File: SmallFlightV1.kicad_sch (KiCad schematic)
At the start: 0 parts

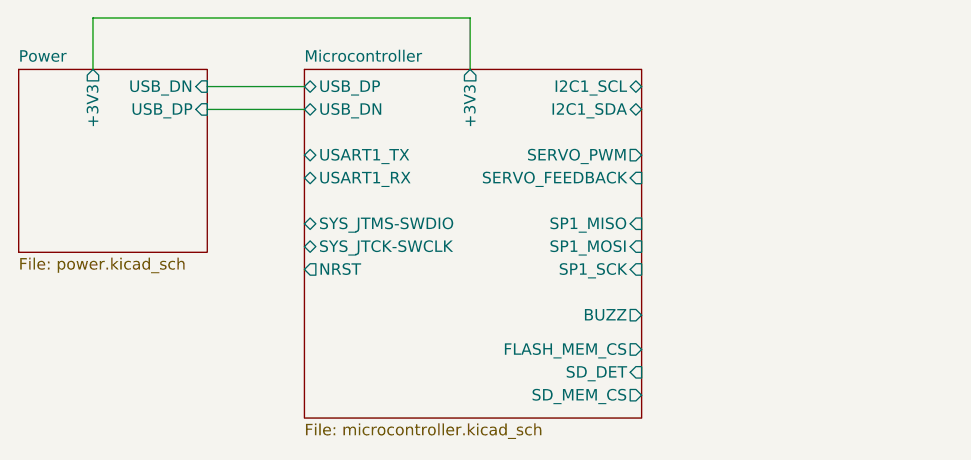
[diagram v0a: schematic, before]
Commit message: Update MCU schematic with VCAP capacitor. Draw boxes around communication busses and programming bus
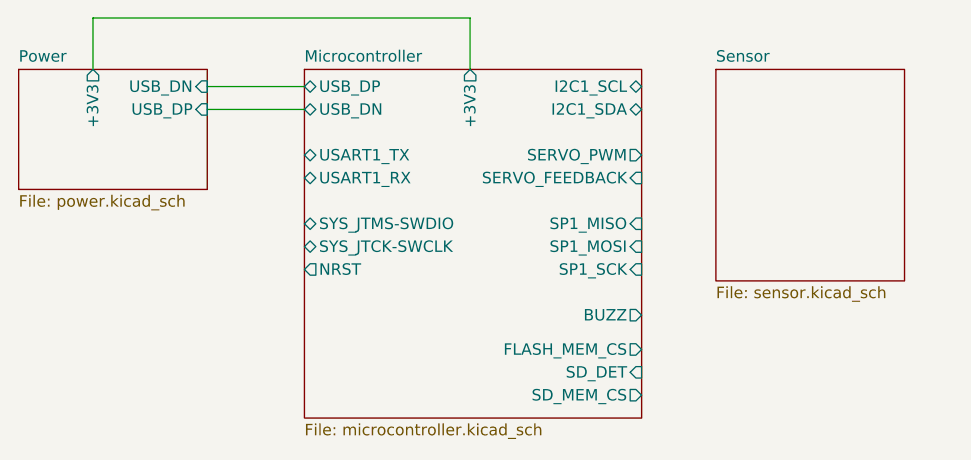
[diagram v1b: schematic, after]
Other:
- added sheet Sensor (sensor.kicad_sch)
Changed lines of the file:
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@@
 (kicad_sch
-	(version 20250114)
+	(version 20260306)
 	(generator "eeschema")
-	(generator_version "9.0")
+	(generator_version "10.0")
 	(paper "A4")
 	(wire
@@
 			(width 0)
 			(type default)
+		)
+	)
+	(sheet
+		(at 170.815 31.115)
+		(size 20.955 23.495)
+		(exclude_from_sim no)
+		(in_bom yes)
+		(on_board yes)
+		(dnp no)
+		(fields_autoplaced yes)
+		(stroke
+			(width 0.1524)
+			(type solid)
+		)
+		(fill
+			(color 0 0 0 0)
+		)
+		(property "Sheetname" "Sensor"
+			(at 170.815 30.4034 0)
+			(show_name no)
+			(do_not_autoplace no)
+			(effects
+				(font
+					(size 1.27 1.27)
+				)
+				(justify left bottom)
+			)
+		)
+		(property "Sheetfile" "sensor.kicad_sch"
+			(at 170.815 55.1946 0)
+			(show_name no)
+			(do_not_autoplace no)
+			(effects
+				(font
+					(size 1.27 1.27)
+				)
+				(justify left top)
+			)
+		)
+		(instances
+			(project "SmallFlightV1"
+				(path "/5a8b04a1-a6d6-48bd-ac5f-d4986cb92d03"
+					(page "4")
+				)
+			)
 		)
 	)
@@
 		)
 		(fill
-			(color 0 0 0 0.0000)
+			(color 0 0 0 0)
 		)
 		(property "Sheetname" "Microcontroller"
 			(at 125.095 30.4034 0)
+			(show_name no)
+			(do_not_autoplace no)
 			(effects
 				(font
@@
 		(property "Sheetfile" "microcontroller.kicad_sch"
 			(at 125.095 70.4346 0)
+			(show_name no)
+			(do_not_autoplace no)
 			(effects
 				(font
@@
 	(sheet
 		(at 93.345 31.115)
-		(size 20.955 20.32)
+		(size 20.955 13.335)
 		(exclude_from_sim no)
 		(in_bom yes)
@@
 		)
 		(fill
-			(color 0 0 0 0.0000)
+			(color 0 0 0 0)
 		)
 		(property "Sheetname" "Power"
 			(at 93.345 30.4034 0)
+			(show_name no)
+			(do_not_autoplace no)
 			(effects
 				(font
@@
 		)
 		(property "Sheetfile" "power.kicad_sch"
-			(at 93.345 52.0196 0)
-			(effects
-				(font
+			(at 93.345 45.0346 0)
+			(show_name no)
+			(do_not_autoplace no)
+			(effects
+				(font

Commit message: remove redundant stm32f44 document folder. remove USB pinouts and references
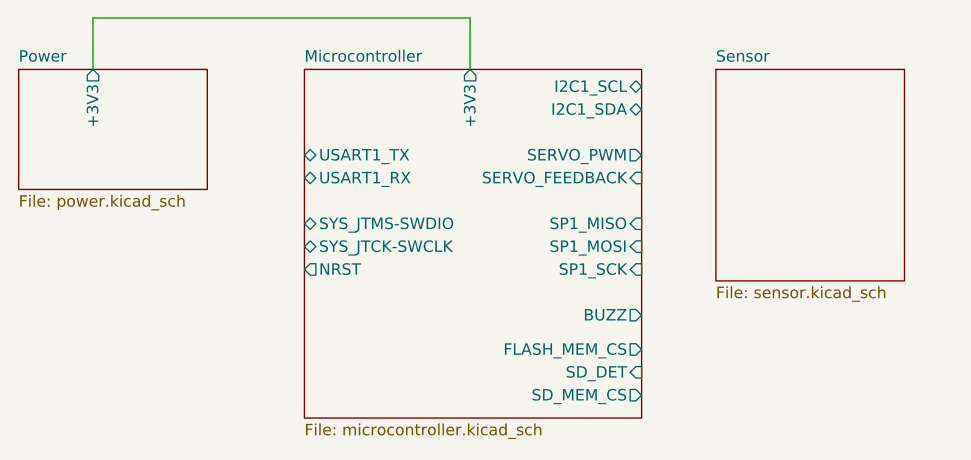
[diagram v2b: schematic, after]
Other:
- sheet Microcontroller ports: added none; removed USB_DN, USB_DP
- sheet Power ports: added none; removed USB_DN, USB_DP
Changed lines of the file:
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@@
-	(wire
-		(pts
-			(xy 114.3 35.56) (xy 125.095 35.56)
-		)
-		(stroke
-			(width 0)
-			(type default)
-		)
-	)
-	(wire
-		(pts
-			(xy 114.3 33.02) (xy 125.095 33.02)
-		)
-		(stroke
-			(width 0)
-			(type default)
-		)
-	)
 	(wire
 		(pts
@@
 			)
 		)
-		(pin "USB_DN" bidirectional
-			(at 125.095 35.56 180)
-			(effects
-				(font
-					(size 1.27 1.27)
-				)
-				(justify left)
-			)
-		)
-		(pin "USB_DP" bidirectional
-			(at 125.095 33.02 180)
-			(effects
-				(font
-					(size 1.27 1.27)
-				)
-				(justify left)
-			)
-		)
 		(pin "SP1_MISO" input
 			(at 162.56 48.26 0)
@@
 			(effects
 				(font
-					(size 1.27 1.27)
-				)
-				(justify right)
-			)
-		)
-		(pin "USB_DN" input
-			(at 114.3 33.02 0)
-			(effects
-				(font
-					(size 1.27 1.27)
-				)
-				(justify right)
-			)
-		)
-		(pin "USB_DP" input
-			(at 114.3 35.56 0)
-			(effects
-				(font

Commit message: fix spi labels. add non connect markers
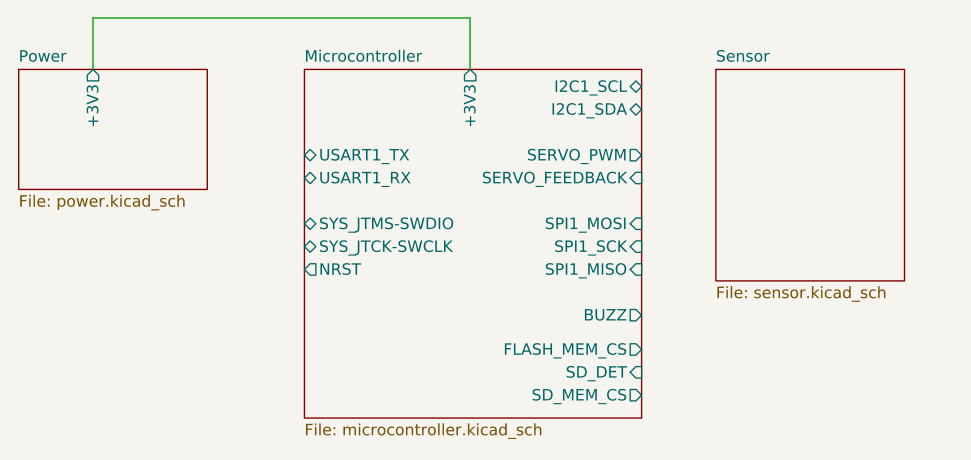
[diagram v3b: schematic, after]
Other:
- sheet Microcontroller ports: added SPI1_MISO, SPI1_MOSI, SPI1_SCK; removed SP1_MISO, SP1_MOSI, SP1_SCK
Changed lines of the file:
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@@
 			)
 		)
-		(pin "SP1_MISO" input
+		(pin "SPI1_MOSI" input
 			(at 162.56 48.26 0)
 			(effects
@@
 			)
 		)
-		(pin "SP1_MOSI" input
+		(pin "SPI1_SCK" input
 			(at 162.56 50.8 0)
 			(effects
@@
 			)
 		)
-		(pin "SP1_SCK" input
+		(pin "SPI1_MISO" input
 			(at 162.56 53.34 0)
 			(effects
